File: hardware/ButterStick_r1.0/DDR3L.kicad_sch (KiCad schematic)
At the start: 14 parts, among them U12 MT41K64M16TW-107_J-TR

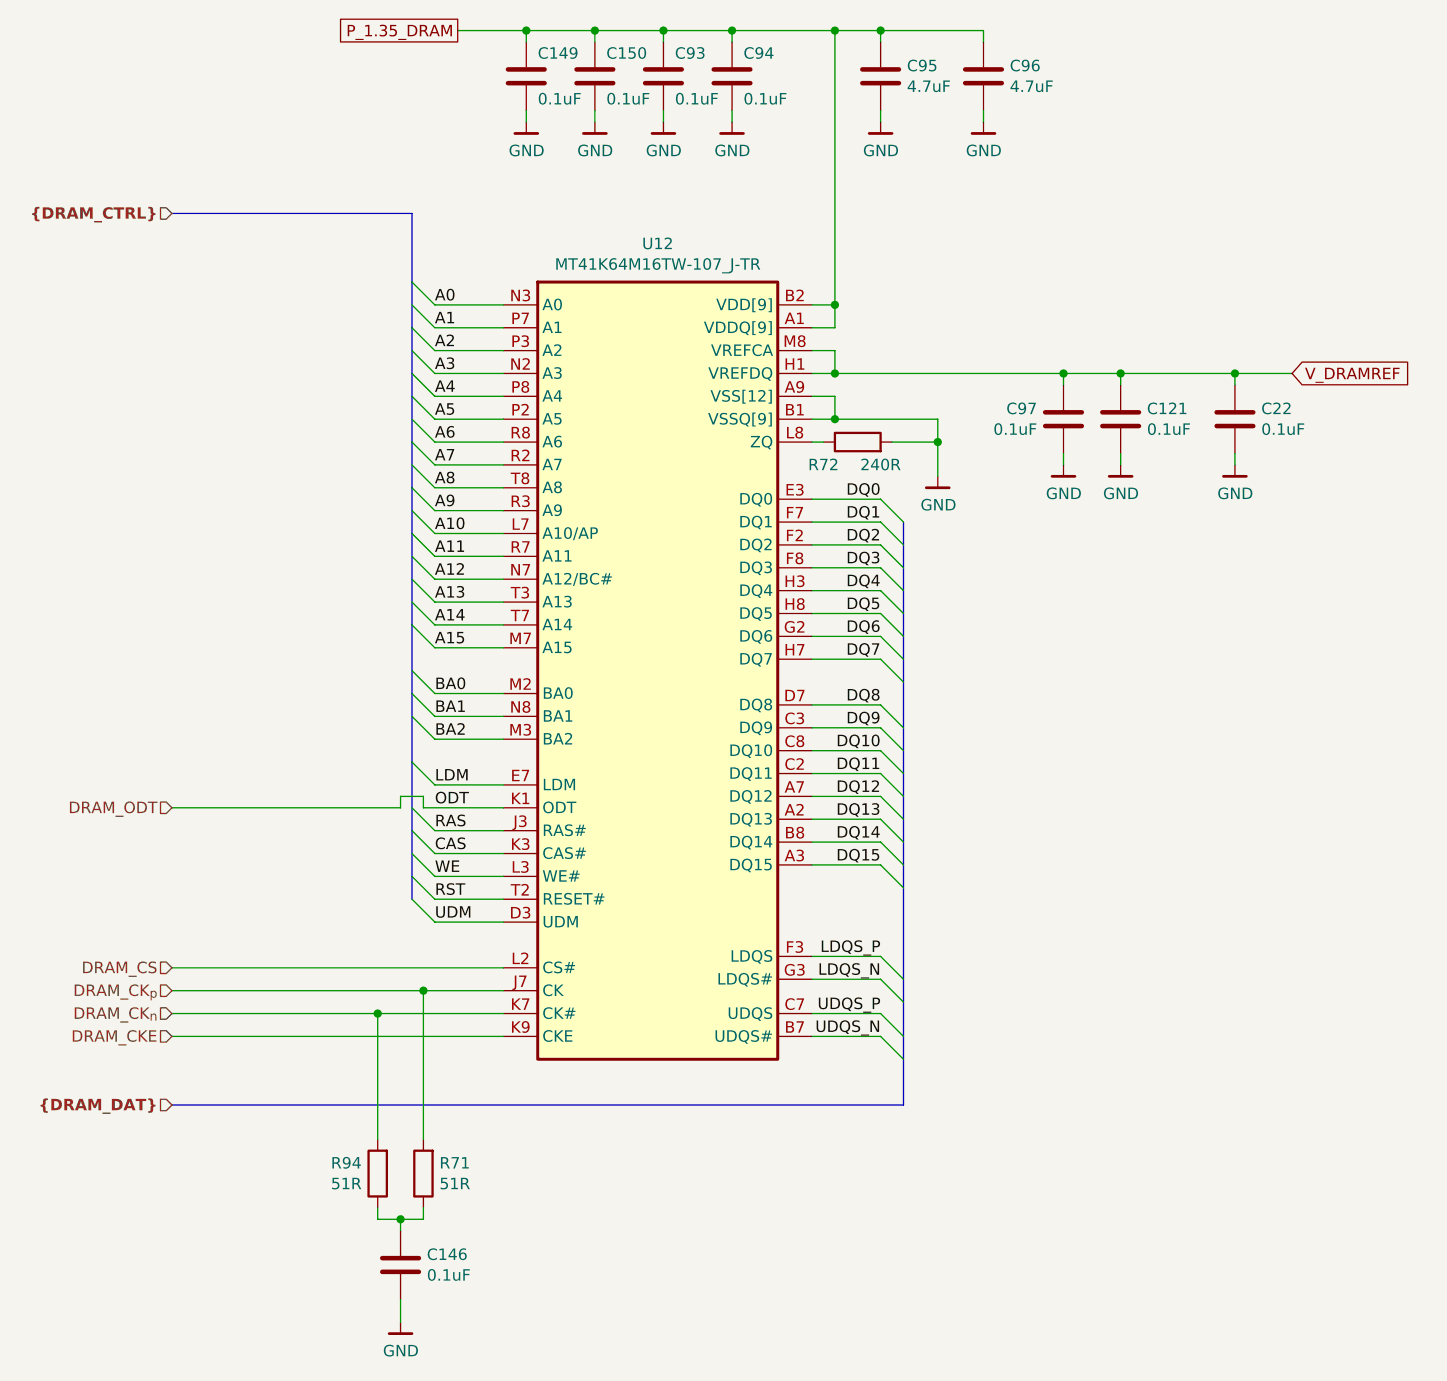
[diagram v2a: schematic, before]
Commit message: hw.r1d0: Fix RGMII straps
This commit correctly sets the stop resistos on the RGMII lines to 1K5
instead of DNP.
Also regenerate and add a schematic in PDF format.

Fixes #6
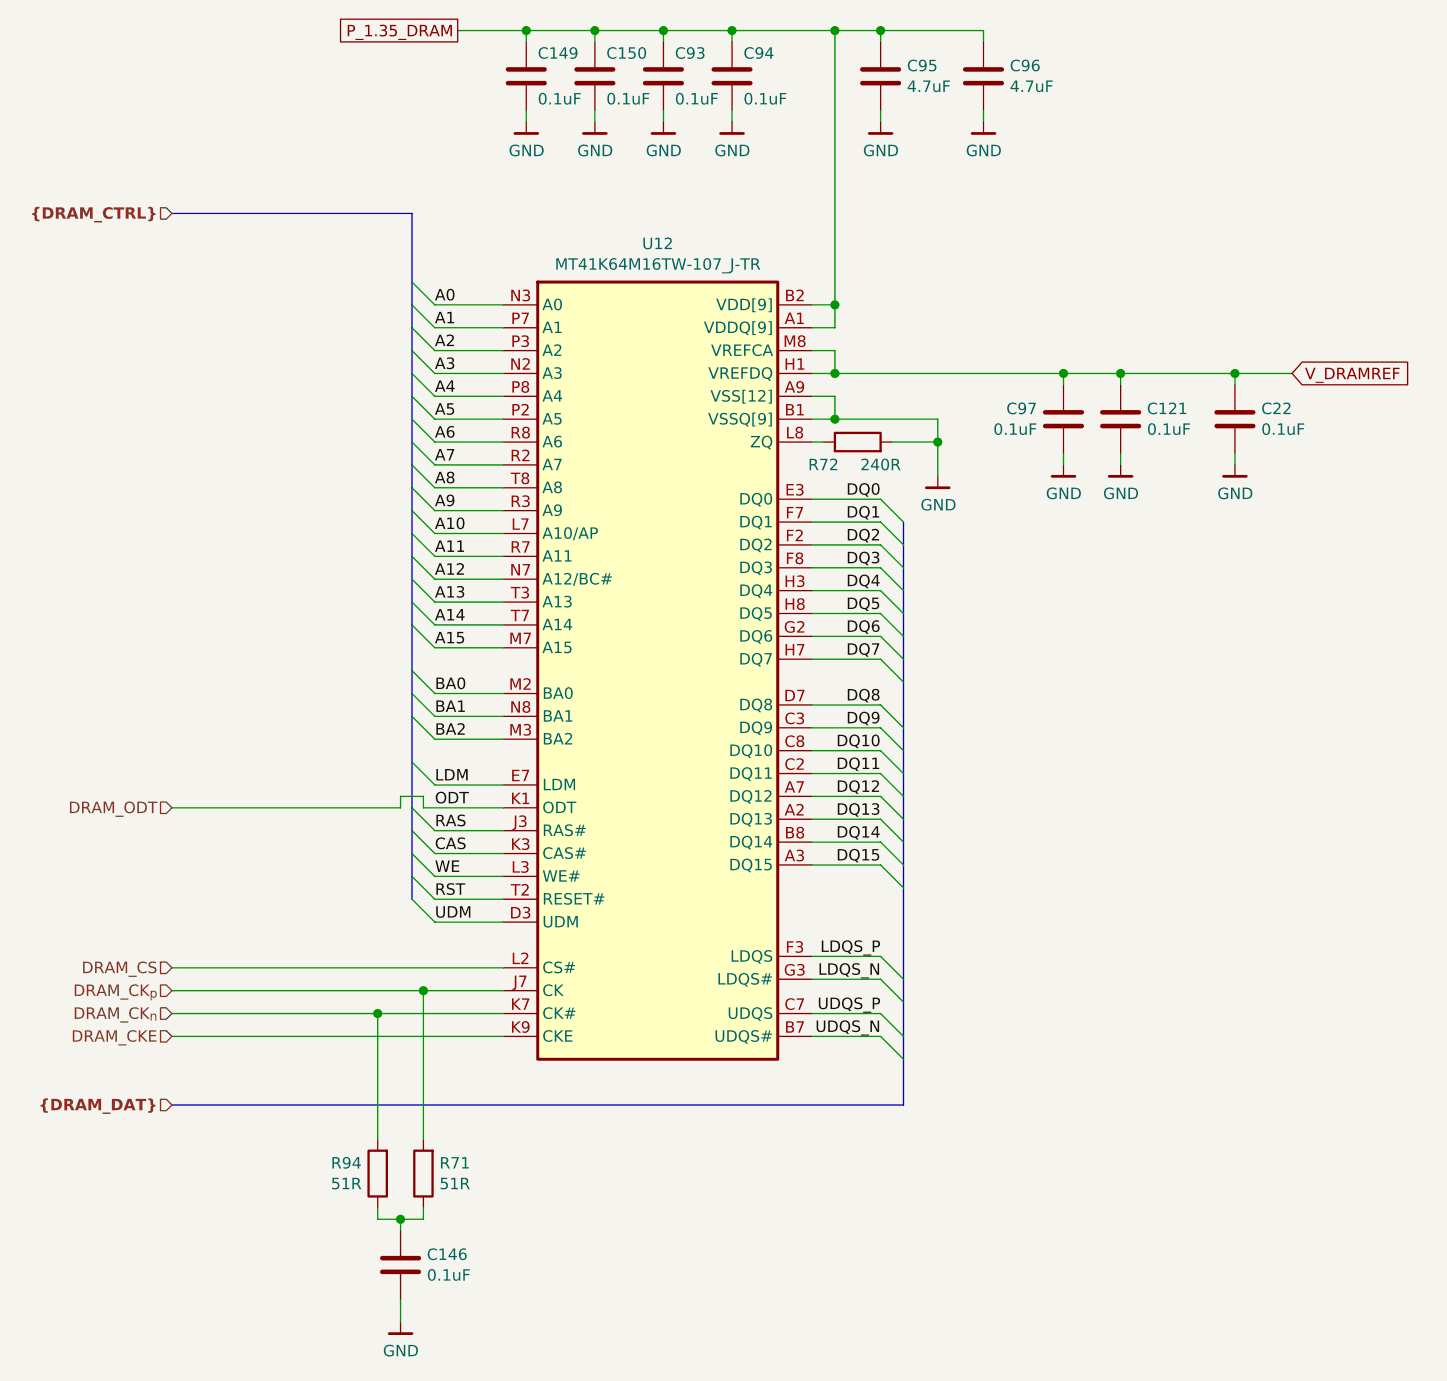
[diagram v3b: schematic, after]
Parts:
- C95, C96: PN CC0402MRX5R6BB475 -> CC0402KRX5R6BB475
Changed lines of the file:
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@@
-(kicad_sch (version 20200618) (host eeschema "5.99.0-unknown-73168a9~101~ubuntu18.04.1")
-  (page 1 18)
+(kicad_sch (version 20201015) (generator eeschema)
+  (page 0 18)
   (paper "A4")
   (title_block
     (title "ButterStick")
-    (date "2020-07-17")
+    (date "2020-11-01")
     (rev "r1.0")
     (company "GsD")
     (comment 1 "Functional prototyping board for the Lattice ECP5.")
-  )
-  (junction (at 106.68 144.78) (diameter 0) (color 0 0 0 0))
-  (junction (at 109.22 167.64) (diameter 0) (color 0 0 0 0))
-  (junction (at 111.76 142.24) (diameter 0) (color 0 0 0 0))
-  (junction (at 123.19 35.56) (diameter 0) (color 0 0 0 0))
-  (junction (at 130.81 35.56) (diameter 0) (color 0 0 0 0))
-  (junction (at 138.43 35.56) (diameter 0) (color 0 0 0 0))
-  (junction (at 146.05 35.56) (diameter 0) (color 0 0 0 0))
-  (junction (at 157.48 35.56) (diameter 0) (color 0 0 0 0))
-  (junction (at 157.48 66.04) (diameter 0) (color 0 0 0 0))
-  (junction (at 157.48 73.66) (diameter 0) (color 0 0 0 0))
-  (junction (at 157.48 78.74) (diameter 0) (color 0 0 0 0))
-  (junction (at 162.56 35.56) (diameter 0) (color 0 0 0 0))
-  (junction (at 168.91 81.28) (diameter 0) (color 0 0 0 0))
-  (junction (at 182.88 73.66) (diameter 0) (color 0 0 0 0))
-  (junction (at 189.23 73.66) (diameter 0) (color 0 0 0 0))
-  (junction (at 201.93 73.66) (diameter 0) (color 0 0 0 0))
+    (comment 2 "SYZYGY compatible")
+  )
+  (junction (at 106.68 144.78) (diameter 1.016) (color 0 0 0 0))
+  (junction (at 109.22 167.64) (diameter 1.016) (color 0 0 0 0))
+  (junction (at 111.76 142.24) (diameter 1.016) (color 0 0 0 0))
+  (junction (at 123.19 35.56) (diameter 1.016) (color 0 0 0 0))
+  (junction (at 130.81 35.56) (diameter 1.016) (color 0 0 0 0))
+  (junction (at 138.43 35.56) (diameter 1.016) (color 0 0 0 0))
+  (junction (at 146.05 35.56) (diameter 1.016) (color 0 0 0 0))
+  (junction (at 157.48 35.56) (diameter 1.016) (color 0 0 0 0))
+  (junction (at 157.48 66.04) (diameter 1.016) (color 0 0 0 0))
+  (junction (at 157.48 73.66) (diameter 1.016) (color 0 0 0 0))
+  (junction (at 157.48 78.74) (diameter 1.016) (color 0 0 0 0))
+  (junction (at 162.56 35.56) (diameter 1.016) (color 0 0 0 0))
+  (junction (at 168.91 81.28) (diameter 1.016) (color 0 0 0 0))
+  (junction (at 182.88 73.66) (diameter 1.016) (color 0 0 0 0))
+  (junction (at 189.23 73.66) (diameter 1.016) (color 0 0 0 0))
+  (junction (at 201.93 73.66) (diameter 1.016) (color 0 0 0 0))
   (bus_entry (at 110.49 63.5) (size 2.54 2.54)
     (stroke (width 0.1524) (type solid) (color 0 0 0 0))
@@
     (stroke (width 0) (type solid) (color 0 0 0 0))
   )
-  (bus (pts (xy 110.49 63.5) (xy 110.49 68.58))
-    (stroke (width 0) (type solid) (color 0 0 0 0))
-  )
-  (bus (pts (xy 110.49 68.58) (xy 110.49 73.66))
+  (bus (pts (xy 110.49 63.5) (xy 110.49 66.04))
+    (stroke (width 0) (type solid) (color 0 0 0 0))
+  )
+  (bus (pts (xy 110.49 66.04) (xy 110.49 68.58))
+    (stroke (width 0) (type solid) (color 0 0 0 0))
+  )
+  (bus (pts (xy 110.49 68.58) (xy 110.49 71.12))
+    (stroke (width 0) (type solid) (color 0 0 0 0))
+  )
+  (bus (pts (xy 110.49 71.12) (xy 110.49 73.66))
     (stroke (width 0) (type solid) (color 0 0 0 0))
   )
@@
     (stroke (width 0) (type solid) (color 0 0 0 0))
   )
-  (bus (pts (xy 110.49 76.2) (xy 110.49 81.28))
-    (stroke (width 0) (type solid) (color 0 0 0 0))
-  )
-  (bus (pts (xy 110.49 81.28) (xy 110.49 86.36))
-    (stroke (width 0) (type solid) (color 0 0 0 0))
-  )
-  (bus (pts (xy 110.49 86.36) (xy 110.49 91.44))
-    (stroke (width 0) (type solid) (color 0 0 0 0))
-  )
-  (bus (pts (xy 110.49 91.44) (xy 110.49 96.52))
-    (stroke (width 0) (type solid) (color 0 0 0 0))
-  )
-  (bus (pts (xy 110.49 96.52) (xy 110.49 101.6))
-    (stroke (width 0) (type solid) (color 0 0 0 0))
-  )
-  (bus (pts (xy 110.49 101.6) (xy 110.49 109.22))
-    (stroke (width 0) (type solid) (color 0 0 0 0))
-  )
-  (bus (pts (xy 110.49 109.22) (xy 110.49 116.84))
-    (stroke (width 0) (type solid) (color 0 0 0 0))
-  )
-  (bus (pts (xy 110.49 116.84) (xy 110.49 124.46))
-    (stroke (width 0) (type solid) (color 0 0 0 0))
-  )
-  (bus (pts (xy 110.49 124.46) (xy 110.49 129.54))
+  (bus (pts (xy 110.49 76.2) (xy 110.49 78.74))
+    (stroke (width 0) (type solid) (color 0 0 0 0))
+  )
+  (bus (pts (xy 110.49 78.74) (xy 110.49 81.28))
+    (stroke (width 0) (type solid) (color 0 0 0 0))
+  )
+  (bus (pts (xy 110.49 81.28) (xy 110.49 83.82))
+    (stroke (width 0) (type solid) (color 0 0 0 0))
+  )
+  (bus (pts (xy 110.49 83.82) (xy 110.49 86.36))
+    (stroke (width 0) (type solid) (color 0 0 0 0))
+  )
+  (bus (pts (xy 110.49 86.36) (xy 110.49 88.9))
+    (stroke (width 0) (type solid) (color 0 0 0 0))
+  )
+  (bus (pts (xy 110.49 88.9) (xy 110.49 91.44))
+    (stroke (width 0) (type solid) (color 0 0 0 0))
+  )
+  (bus (pts (xy 110.49 91.44) (xy 110.49 93.98))
+    (stroke (width 0) (type solid) (color 0 0 0 0))
+  )
+  (bus (pts (xy 110.49 93.98) (xy 110.49 96.52))
+    (stroke (width 0) (type solid) (color 0 0 0 0))
+  )
+  (bus (pts (xy 110.49 96.52) (xy 110.49 99.06))
+    (stroke (width 0) (type solid) (color 0 0 0 0))
+  )
+  (bus (pts (xy 110.49 99.06) (xy 110.49 101.6))
+    (stroke (width 0) (type solid) (color 0 0 0 0))
+  )
+  (bus (pts (xy 110.49 101.6) (xy 110.49 106.68))
+    (stroke (width 0) (type solid) (color 0 0 0 0))
+  )
+  (bus (pts (xy 110.49 106.68) (xy 110.49 109.22))
+    (stroke (width 0) (type solid) (color 0 0 0 0))
+  )
+  (bus (pts (xy 110.49 109.22) (xy 110.49 111.76))
+    (stroke (width 0) (type solid) (color 0 0 0 0))
+  )
+  (bus (pts (xy 110.49 111.76) (xy 110.49 116.84))
+    (stroke (width 0) (type solid) (color 0 0 0 0))
+  )
+  (bus (pts (xy 110.49 116.84) (xy 110.49 121.92))
+    (stroke (width 0) (type solid) (color 0 0 0 0))
+  )
+  (bus (pts (xy 110.49 121.92) (xy 110.49 124.46))
+    (stroke (width 0) (type solid) (color 0 0 0 0))
+  )
+  (bus (pts (xy 110.49 124.46) (xy 110.49 127))
+    (stroke (width 0) (type solid) (color 0 0 0 0))
+  )
+  (bus (pts (xy 110.49 127) (xy 110.49 129.54))
     (stroke (width 0) (type solid) (color 0 0 0 0))
   )
@@
     (stroke (width 0) (type solid) (color 0 0 0 0))
   )
-  (bus (pts (xy 165.1 90.17) (xy 165.1 95.25))
+  (bus (pts (xy 165.1 90.17) (xy 165.1 92.71))
+    (stroke (width 0) (type solid) (color 0 0 0 0))
+  )
+  (bus (pts (xy 165.1 92.71) (xy 165.1 95.25))
     (stroke (width 0) (type solid) (color 0 0 0 0))
   )
@@
     (stroke (width 0) (type solid) (color 0 0 0 0))
   )
-  (bus (pts (xy 165.1 97.79) (xy 165.1 102.87))
+  (bus (pts (xy 165.1 97.79) (xy 165.1 100.33))
+    (stroke (width 0) (type solid) (color 0 0 0 0))
+  )
+  (bus (pts (xy 165.1 100.33) (xy 165.1 102.87))
     (stroke (width 0) (type solid) (color 0 0 0 0))
   )
@@
     (stroke (width 0) (type solid) (color 0 0 0 0))
   )
-  (bus (pts (xy 165.1 105.41) (xy 165.1 113.03))
-    (stroke (width 0) (type solid) (color 0 0 0 0))
-  )
-  (bus (pts (xy 165.1 113.03) (xy 165.1 118.11))
-    (stroke (width 0) (type solid) (color 0 0 0 0))
-  )
-  (bus (pts (xy 165.1 118.11) (xy 165.1 123.19))
-    (stroke (width 0) (type solid) (color 0 0 0 0))
-  )
-  (bus (pts (xy 165.1 123.19) (xy 165.1 128.27))
-    (stroke (width 0) (type solid) (color 0 0 0 0))
-  )
-  (bus (pts (xy 165.1 128.27) (xy 165.1 140.97))
-    (stroke (width 0) (type solid) (color 0 0 0 0))
-  )
-  (bus (pts (xy 165.1 140.97) (xy 165.1 147.32))
-    (stroke (width 0) (type solid) (color 0 0 0 0))
-  )
-  (bus (pts (xy 165.1 147.32) (xy 165.1 154.94))
+  (bus (pts (xy 165.1 105.41) (xy 165.1 107.95))
+    (stroke (width 0) (type solid) (color 0 0 0 0))
+  )
+  (bus (pts (xy 165.1 107.95) (xy 165.1 113.03))
+    (stroke (width 0) (type solid) (color 0 0 0 0))
+  )
+  (bus (pts (xy 165.1 113.03) (xy 165.1 115.57))
+    (stroke (width 0) (type solid) (color 0 0 0 0))
+  )
+  (bus (pts (xy 165.1 115.57) (xy 165.1 118.11))
+    (stroke (width 0) (type solid) (color 0 0 0 0))
+  )
+  (bus (pts (xy 165.1 118.11) (xy 165.1 120.65))
+    (stroke (width 0) (type solid) (color 0 0 0 0))
+  )
+  (bus (pts (xy 165.1 120.65) (xy 165.1 123.19))
+    (stroke (width 0) (type solid) (color 0 0 0 0))
+  )
+  (bus (pts (xy 165.1 123.19) (xy 165.1 125.73))
+    (stroke (width 0) (type solid) (color 0 0 0 0))
+  )
+  (bus (pts (xy 165.1 125.73) (xy 165.1 128.27))
+    (stroke (width 0) (type solid) (color 0 0 0 0))
+  )
+  (bus (pts (xy 165.1 128.27) (xy 165.1 130.81))
+    (stroke (width 0) (type solid) (color 0 0 0 0))
+  )
+  (bus (pts (xy 165.1 130.81) (xy 165.1 140.97))
+    (stroke (width 0) (type solid) (color 0 0 0 0))
+  )
+  (bus (pts (xy 165.1 140.97) (xy 165.1 143.51))
+    (stroke (width 0) (type solid) (color 0 0 0 0))
+  )
+  (bus (pts (xy 165.1 143.51) (xy 165.1 147.32))
+    (stroke (width 0) (type solid) (color 0 0 0 0))
+  )
+  (bus (pts (xy 165.1 147.32) (xy 165.1 149.86))
+    (stroke (width 0) (type solid) (color 0 0 0 0))
+  )
+  (bus (pts (xy 165.1 149.86) (xy 165.1 154.94))
     (stroke (width 0) (type solid) (color 0 0 0 0))
   )
@@
       (effects (font (size 1.27 1.27)) hide)
     )
-    (property "PN" "CC0402MRX5R6BB475" (id 4) (at 162.56 40.64 0)
+    (property "PN" "CC0402KRX5R6BB475" (id 4) (at 162.56 40.64 0)
       (effects (font (size 1.27 1.27)) hide)
     )
@@
       (effects (font (size 1.27 1.27)) hide)
     )
-    (property "PN" "CC0402MRX5R6BB475" (id 4) (at 173.99 40.64 0)
-      (effects (font (size 1.27 1.27)) hide)
-    )
+    (property "PN" "CC0402KRX5R6BB475" (id 4) (at 173.99 40.64 0)
+      (effects (font (size 1.27 1.27)) hide)
+    )
